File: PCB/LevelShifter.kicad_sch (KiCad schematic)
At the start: 106 parts, among them J1 POWER, J10 M2, J11 M1, J12 Selector, J13 M0, J14 M_FEED, J15 M_FEED, J16 M_FEED, J17 Selector, J18 OUTPUT, J19 OUT0, J2 INPUT, J20 OUT1, J21 OUT2, J22 OUT3, J23 IN0, J24 IN1, J25 IN2, J26 IN3, J27 ROBOT, J28 ZIF, J3 ANALOG0, J4 ANALOG1, J5 ANALOG2, J6 ANALOG3, J7 DE9_Plug_MountingHoles, J8 SPECIAL, J9 RESET, Q1 IRF540N, Q2 IRF540N, Q3 IRF540N, U1 LM324A, U10 PC817, U2 MAX232, U3 PC817, U4 PC817, U5 PC817, U6 PC817, U7 PC817, U8 PC817, U9 PC817

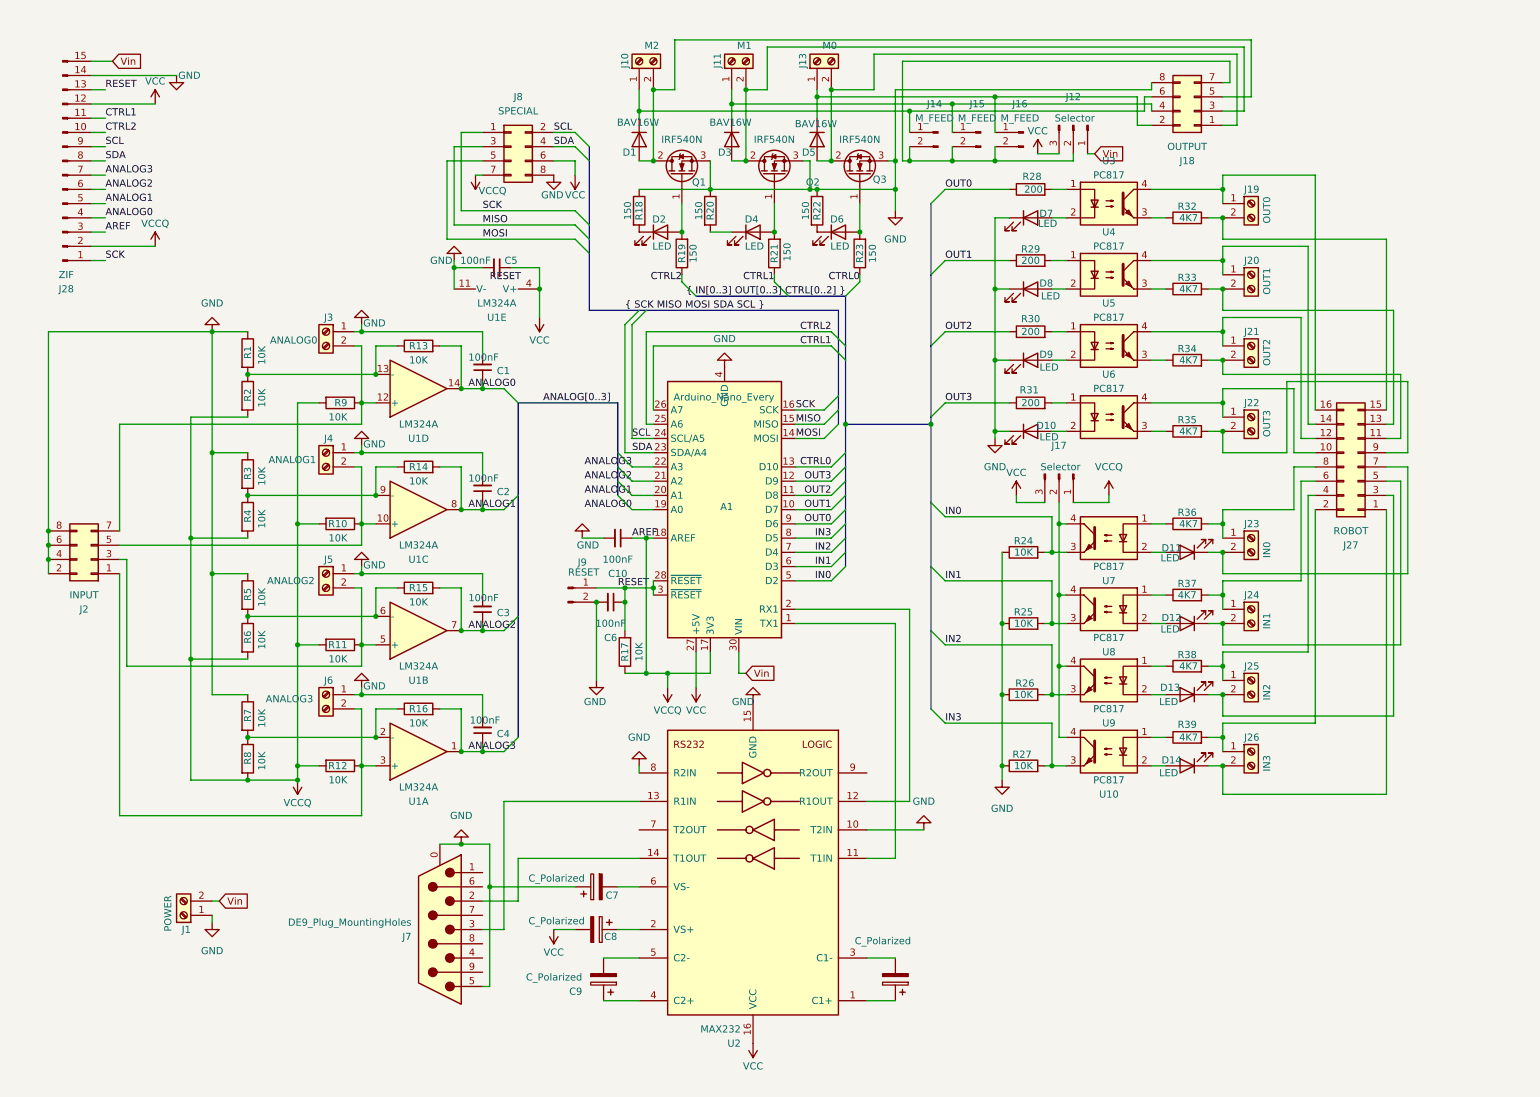
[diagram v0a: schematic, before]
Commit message: [ARDUINO] Make PWM available for Servo motor (5V from buck circuit. PW on pinout) [PICO] Allow design for RaspberryPi Pico placement
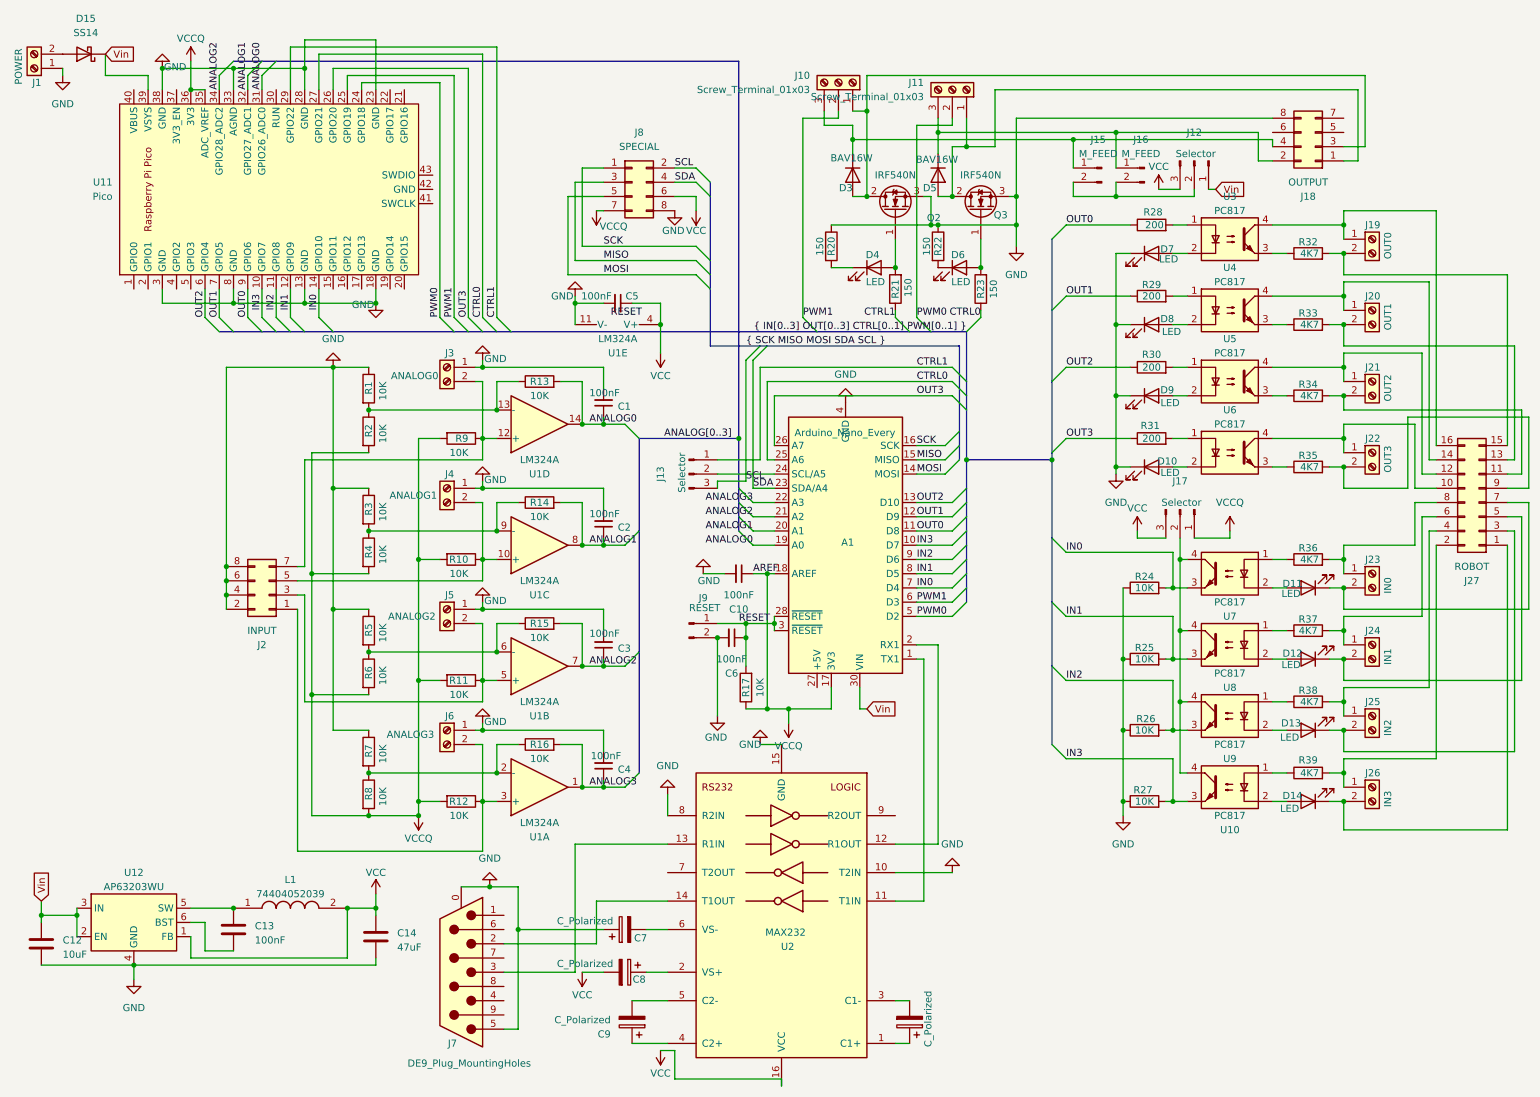
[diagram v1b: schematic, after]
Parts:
- removed D1: BAV16W, Diode_SMD:D_SOD-123, symbol Diode:BAV16W
- removed D2: LED, LED_THT:LED_D5.0mm, symbol Device:LED
- removed J10: M2, TerminalBlock_MetzConnect:TerminalBlock_MetzConnect_Type101_RT01602HBWC_1x02_P5.08mm_Horizontal, symbol Connector:Screw_Terminal_01x02
- removed J11: M1, TerminalBlock_MetzConnect:TerminalBlock_MetzConnect_Type101_RT01602HBWC_1x02_P5.08mm_Horizontal, symbol Connector:Screw_Terminal_01x02
- removed J13: M0, TerminalBlock_MetzConnect:TerminalBlock_MetzConnect_Type101_RT01602HBWC_1x02_P5.08mm_Horizontal, symbol Connector:Screw_Terminal_01x02
- removed J14: M_FEED, Connector_PinSocket_2.54mm:PinSocket_1x02_P2.54mm_Vertical, symbol Connector:Conn_01x02_Pin
- removed J28: ZIF, Connector_PinHeader_2.54mm:PinHeader_1x15_P2.54mm_Vertical, symbol Connector:Conn_01x15_Pin
- removed Q1: IRF540N, Package_TO_SOT_THT:TO-220-3_Vertical, symbol Transistor_FET:IRF540N
- removed R18, R19: 150, Resistor_THT:R_Axial_DIN0207_L6.3mm_D2.5mm_P7.62mm_Horizontal, symbol Device:R
- added C12: 10uF, Capacitor_SMD:C_0805_2012Metric_Pad1.18x1.45mm_HandSolder, symbol Device:C
- added C13: 100nF, Capacitor_SMD:C_0805_2012Metric_Pad1.18x1.45mm_HandSolder, symbol Device:C
- added C14: 47uF, Capacitor_SMD:C_0805_2012Metric_Pad1.18x1.45mm_HandSolder, symbol Device:C
- added D15: SS14, Diode_SMD:D_SMA, symbol Diode:SS14
- added J10, J11: Screw_Terminal_01x03, TerminalBlock_MetzConnect:TerminalBlock_MetzConnect_Type011_RT05503HBWC_1x03_P5.00mm_Horizontal, symbol Connector:Screw_Terminal_01x03
- added J13: Selector, Connector_PinHeader_2.54mm:PinHeader_1x03_P2.54mm_Vertical, symbol Connector:Conn_01x03_Pin
- added L1: 74404052039, footprints:74404052039, symbol 74404052039:74404052039
- added U11: Pico, Components:pico, symbol PICO:Pico
- added U12: AP63203WU, Package_TO_SOT_SMD:TSOT-23-6, symbol Regulator_Switching:AP63203WU
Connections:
- net CTRL2 is gone; now on net CTRL0: A1.25 (A6)
- net ANALOG0: now also U11.31 (GPIO26_ADC0)
- net ANALOG1: now also U11.32 (GPIO27_ADC1)
- net ANALOG2: now also U11.34 (GPIO28_ADC2)
- net CTRL0: now also U11.27 (GPIO21); no longer A1.13 (D10)
- net CTRL1: now also J13.1 (Pin_1), U11.29 (GPIO22); no longer A1.26 (A7)
- net GND: now also C12.2, C14.2, U11.13 (GND), U11.18 (GND), U11.23 (GND), U11.28 (GND), U11.3 (GND), U11.33 (AGND), U11.38 (GND), U11.8 (GND), U12.4 (GND)
- net IN0: now also A1.7 (D4), U11.14 (GPIO10); no longer A1.5 (D2)
- net IN1: now also A1.8 (D5), U11.12 (GPIO9); no longer A1.6 (D3)
- net IN2: now also A1.9 (D6), U11.11 (GPIO8); no longer A1.7 (D4)
- net IN3: now also A1.10 (D7), U11.10 (GPIO7); no longer A1.8 (D5)
- net OUT0: now also A1.11 (D8), U11.9 (GPIO6); no longer A1.9 (D6)
- net OUT1: now also A1.12 (D9), U11.7 (GPIO5); no longer A1.10 (D7)
- net OUT2: now also A1.13 (D10), U11.6 (GPIO4); no longer A1.11 (D8)
- net OUT3: now also A1.26 (A7), U11.26 (GPIO20); no longer A1.12 (D9)
- net SCL: now also J13.3 (Pin_3); no longer A1.24 (SCL/A5)
- net VCC: now also C14.1, L1.2, U12.1 (FB); no longer A1.27 (+5V)
- net VCCQ: now also U11.35 (ADC_VREF), U11.36 (3V3)
- net Vin: now also C12.1, D15.1 (K), U11.39 (VSYS), U12.2 (EN), U12.3 (IN); no longer J1.2 (Pin_2)
- net at D5.1 (K), J16.1 (Pin_1), J18.2 (Pin_2): now also J11.3 (Pin_3)
- net at D5.2 (A), J18.1 (Pin_1), Q3.2 (D): now also J11.1 (Pin_1)
- net at J12.2 (Pin_2), J15.2 (Pin_2), J16.2 (Pin_2): no longer J18.7 (Pin_7)
- net at D3.1 (K), J15.1 (Pin_1), J18.4 (Pin_4): now also J10.3 (Pin_3)
- net at D3.2 (A), J18.3 (Pin_3), Q2.2 (D): now also J10.1 (Pin_1)
- new net: C13.1, L1.1, U12.5 (SW)
- new net: C13.2, U12.6 (BST)
- new net: A1.24 (SCL/A5), J13.2 (Pin_2)
- new net: D15.2 (A), J1.2 (Pin_2)
- new net PWM0: A1.5 (D2), J11.2 (Pin_2), U11.24 (GPIO18)
- new net PWM1: A1.6 (D3), J10.2 (Pin_2), U11.25 (GPIO19)
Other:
- moved on the sheet: A1, C1, C10, C2, C3, C4, C5, C6, C7, C8, C9, D10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

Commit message: [UPDATE] outing done. Start the final touch!
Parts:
- added J14: Serial, Connector_PinSocket_2.54mm:PinSocket_1x04_P2.54mm_Vertical, symbol Connector:Conn_01x04_Pin
- J7: footprint Connector_Dsub:DSUB-9_Male_Horizontal_P2.77x2.84mm_EdgePinOffset4.94mm_Housed_MountingHolesOffset7.48mm -> Connector_Dsub:DSUB-9_Female_Horizontal_P2.77x2.84mm_EdgePinOffset4.94mm_Housed_MountingHolesOffset7.48mm
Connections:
- net GND: now also J14.1 (Pin_1), J14.4 (Pin_4)
- net MISO: now also U11.6 (GPIO4)
- net MOSI: now also U11.5 (GPIO3)
- net OUT2: now also U11.25 (GPIO19); no longer U11.6 (GPIO4)
- net PWM0: now also J18.6 (Pin_6), U11.22 (GPIO17); no longer U11.24 (GPIO18)
- net PWM1: now also J18.5 (Pin_5), U11.24 (GPIO18); no longer U11.25 (GPIO19)
- net SCK: now also U11.4 (GPIO2)
- net SCL: now also U11.20 (GPIO15)
- net SDA: now also U11.19 (GPIO14)
- net at A1.1 (TX1), U2.11 (T1IN): now also U11.1 (GPIO0), J14.2 (Pin_2)
- net at A1.2 (RX1), U2.12 (R1OUT): now also U11.2 (GPIO1), J14.3 (Pin_3)
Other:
- moved on the sheet: J3, R13

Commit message: [COMPLETED] All tracks laid. Wiaitng for the production of the PCB.
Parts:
- L1: footprint footprints:74404052039 -> Components:CD75
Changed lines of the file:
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@@
 			)
 		)
-		(property "Footprint" "footprints:74404052039"
+		(property "Footprint" "Components:CD75"
 			(at 68.58 263.83 0)
 			(effects

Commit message: [TESTED]
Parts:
- removed C11, C7, C8, C9: C_Polarized, Capacitor_THT:CP_Radial_D6.3mm_P2.50mm, symbol Device:C_Polarized
- added C11, C7, C8, C9: 1uF, Capacitor_SMD:C_1206_3216Metric_Pad1.33x1.80mm_HandSolder, symbol Device:C
- added J28: M_FEED, Connector_PinSocket_2.54mm:PinSocket_1x02_P2.54mm_Vertical, symbol Connector:Conn_01x02_Pin
- C12, C14: footprint Capacitor_SMD:C_0805_2012Metric_Pad1.18x1.45mm_HandSolder -> Capacitor_SMD:C_1206_3216Metric_Pad1.33x1.80mm_HandSolder
- U12: value AP63203WU -> AP63205WU
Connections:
- net SDA is gone; now on net ANALOG[0..3]: A1.23 (SDA/A4), J8.4 (Pin_4), U11.19 (GPIO14)
- net ANALOG0: now also A1.25 (A6); no longer A1.19 (A0)
- net ANALOG1: now also A1.22 (A3); no longer A1.20 (A1)
- net ANALOG3: now also A1.26 (A7); no longer A1.22 (A3)
- net CTRL0: now also A1.20 (A1); no longer A1.25 (A6)
- net CTRL1: now also J28.2 (Pin_2)
- net GND: now also C7.1
- net IN0: now also A1.5 (D2); no longer A1.7 (D4)
- net IN1: now also A1.6 (D3); no longer A1.8 (D5)
- net IN2: now also A1.7 (D4); no longer A1.9 (D6)
- net OUT3: now also A1.19 (A0); no longer A1.26 (A7)
- net PWM0: now also A1.8 (D5); no longer A1.5 (D2)
- net PWM1: now also A1.9 (D6); no longer A1.6 (D3)
- net VCC: now also U11.39 (VSYS), C8.1, J28.1 (Pin_1)
- net Vin: no longer U11.39 (VSYS)
- net at U2.1 (C1+): now also C11.1
- net at U2.3 (C1-): now also C11.2
- net at U2.2 (VS+): now also C8.2
- net at U2.4 (C2+): now also C9.1
- net at U2.5 (C2-): now also C9.2
- net at U2.6 (VS-): now also C7.2

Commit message: [SYNC]
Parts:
- R20, R21, R22, R23: value 150 -> 100
- R24, R25, R26, R27: value 10K -> 47K
- R28, R29, R30, R31: value 200 -> 100
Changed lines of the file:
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@@
 			)
 		)
-		(property "Value" "200"
+		(property "Value" "100"
 			(at 215.9 71.12 90)
 			(effects
@@
 			)
 		)
-		(property "Value" "150"
+		(property "Value" "100"
 			(at 172.466 56.896 90)
 			(effects
@@
 			)
 		)
-		(property "Value" "10K"
+		(property "Value" "47K"
 			(at 214.63 135.89 90)
 			(effects
@@
 			)
 		)
-		(property "Value" "150"
+		(property "Value" "100"
 			(at 175.768 49.53 90)
 			(effects
@@
 			)
 		)
-		(property "Value" "10K"
+		(property "Value" "47K"
 			(at 214.63 123.19 90)
 			(effects
@@
 			)
 		)
-		(property "Value" "200"
+		(property "Value" "100"
 			(at 216.408 45.72 90)
 			(effects
@@
 			)
 		)
-		(property "Value" "150"
+		(property "Value" "100"
 			(at 156.718 49.53 90)
 			(effects
@@
 			)
 		)
-		(property "Value" "200"
+		(property "Value" "100"
 			(at 215.9 83.82 90)
 			(effects
@@
 			)
 		)
-		(property "Value" "10K"
+		(property "Value" "47K"
 			(at 214.63 148.59 90)
 			(effects
@@
 			)
 		)
-		(property "Value" "150"
+		(property "Value" "100"
 			(at 187.706 57.15 90)
 			(effects
@@
 			)
 		)
-		(property "Value" "10K"
+		(property "Value" "47K"
 			(at 214.63 110.49 90)
 			(effects
@@
 			)
 		)
-		(property "Value" "200"
+		(property "Value" "100"
 			(at 215.9 58.42 90)
 			(effects
